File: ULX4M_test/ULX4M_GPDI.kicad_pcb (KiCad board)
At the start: 4 copper layers, 60 x 74 mm, 24 parts, among them J1 DF40C-100DP-0.4V(51), J10 DF40C-100DP-0.4V(51), J11 DF40C-100DP-0.4V(51), J12 DF40C-100DP-0.4V(51), J2 DF40C-100DP-0.4V(51), J3 DF40C-100DP-0.4V(51), J4 DF40C-100DP-0.4V(51), J5 DF40C-100DS-0.4V(51), J6 DF40C-100DS-0.4V(51), J7 DF40C-100DS-0.4V(51), J8 DF40C-100DS-0.4V(51), J9 DF40C-100DP-0.4V(51), P1 HDMI-D, P2 HDMI-D, P3 HDMI-D, P4 HDMI-D

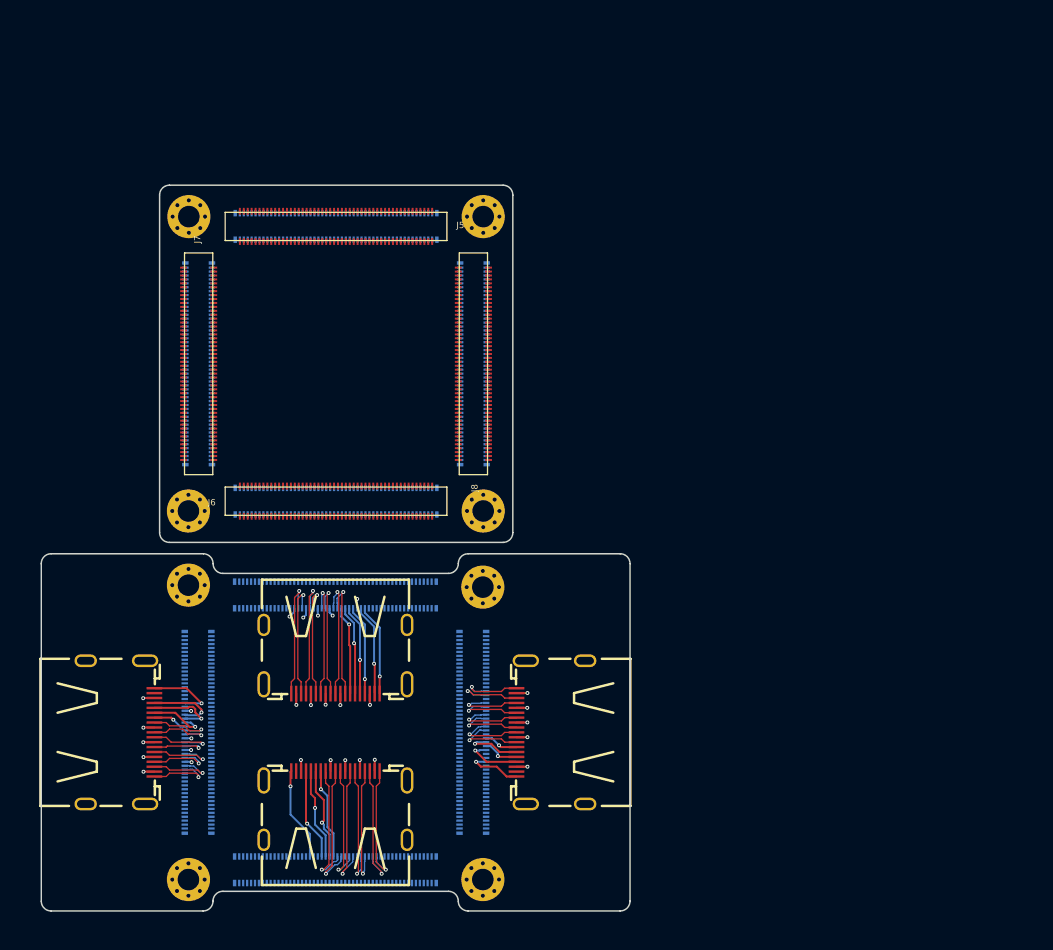
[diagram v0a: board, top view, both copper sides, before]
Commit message: Changing PCB size
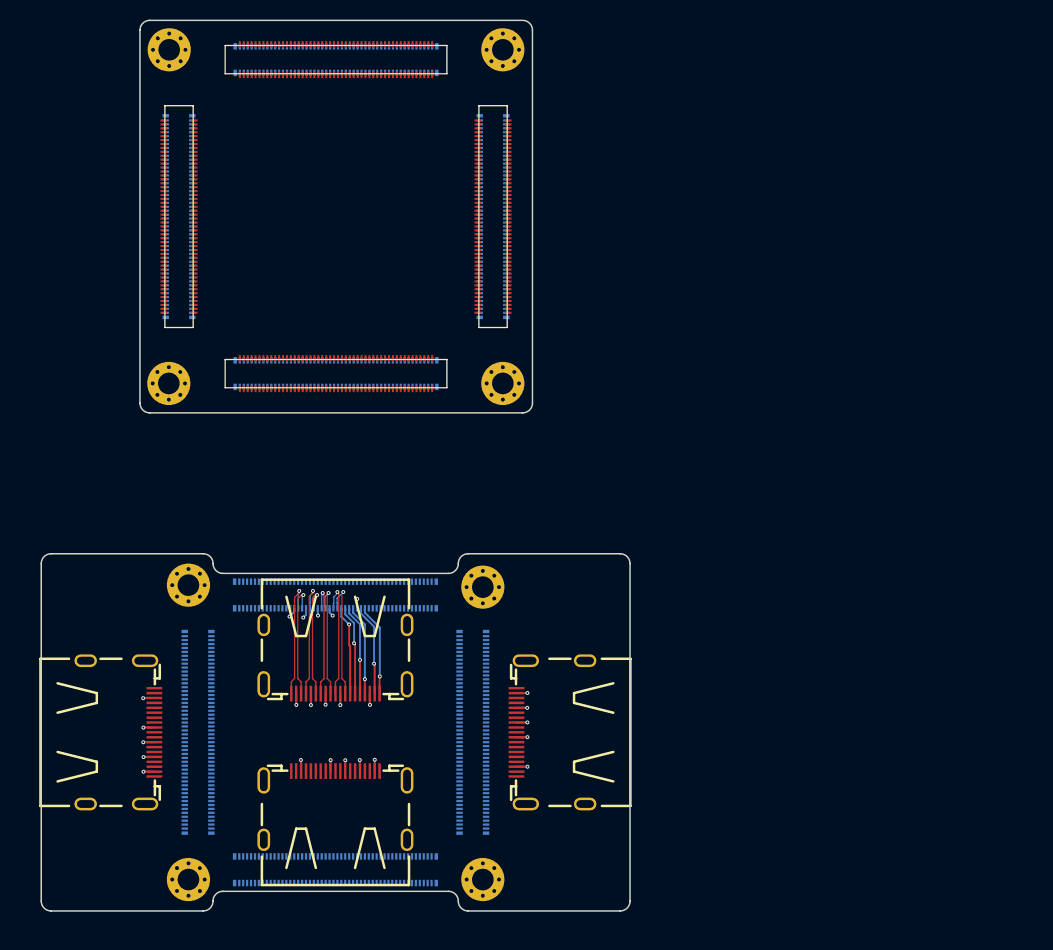
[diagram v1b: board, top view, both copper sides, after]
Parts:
- moved H5 17.1 mm to (83.1, 20.4)
- moved H7 17.1 mm to (117.1, 20.4)
- moved J5 17.0 mm to (100.1, 21.4)
- moved J9 17.0 mm to (100.1, 21.4)
- moved J11 15.1 mm to (84.1, 37.4)
- moved J12 15.1 mm to (116.1, 37.4)
- moved J7 15.1 mm to (84.1, 37.4)
- moved J8 15.1 mm to (116.1, 37.4)
- moved H6 13.2 mm to (83.0, 54.4)
- moved H8 13.2 mm to (117.1, 54.4)
- moved J10 13.0 mm to (100.1, 53.4)
- moved J6 13.0 mm to (100.1, 53.4)
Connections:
- J2 pad 36: (no net) -> P2_ETH-
- J2 pad 38: P2_ETH- -> +5V
- J2 pad 40: +5V -> GND
- J2 pad 42: GND -> P2_SDA
- J2 pad 44: P2_SDA -> P2_SCL
- J2 pad 46: P2_SCL -> P2_ETH+
- J2 pad 48: P2_ETH+ -> P2_CEC
- J2 pad 50: P2_CEC -> P2_CLK-
- J2 pad 52: P2_CLK- -> P2_CLK+
- J2 pad 54: P2_CLK+ -> GND
- J2 pad 56: (no net) -> P2_D0-
- J2 pad 58: P2_D0- -> P2_D0+
- J2 pad 60: P2_D0+ -> GND
- J2 pad 62: (no net) -> P2_D1-
- J2 pad 64: P2_D1- -> P2_D1+
- J2 pad 66: P2_D1+ -> GND
- J2 pad 68: (no net) -> P2_D2-
- J2 pad 70: P2_D2- -> P2_D2+
- J2 pad 72: P2_D2+ -> GND
- J3 pad 35: P3_ETH- -> (no net)
- J3 pad 36: (no net) -> P3_ETH-
- J3 pad 37: +5V -> (no net)
- J3 pad 38: (no net) -> +5V
- J3 pad 39: GND -> (no net)
- J3 pad 40: (no net) -> GND
- J3 pad 41: P3_SDA -> (no net)
- J3 pad 42: (no net) -> P3_SDA
- J3 pad 43: P3_SCL -> (no net)
- J3 pad 44: (no net) -> P3_SCL
- J3 pad 45: P3_ETH+ -> (no net)
- J3 pad 46: (no net) -> P3_ETH+
- J3 pad 47: P3_CEC -> (no net)
- J3 pad 48: (no net) -> P3_CEC
- J3 pad 49: P3_CLK- -> (no net)
- J3 pad 50: (no net) -> P3_CLK-
- J3 pad 51: P3_CLK+ -> (no net)
- J3 pad 52: (no net) -> P3_CLK+
- J3 pad 53: GND -> (no net)
- J3 pad 54: (no net) -> GND
- J3 pad 55: P3_D0- -> (no net)
- J3 pad 56: (no net) -> P3_D0-
- J3 pad 57: P3_D0+ -> (no net)
- J3 pad 58: (no net) -> P3_D0+
- J3 pad 59: GND -> (no net)
- J3 pad 60: (no net) -> GND
- J3 pad 61: P3_D1- -> (no net)
- J3 pad 62: (no net) -> P3_D1-
- J3 pad 63: P3_D1+ -> (no net)
- J3 pad 64: (no net) -> P3_D1+
- J3 pad 65: GND -> (no net)
- J3 pad 66: (no net) -> GND
- J3 pad 67: P3_D2- -> (no net)
- J3 pad 68: (no net) -> P3_D2-
- J3 pad 69: P3_D2+ -> (no net)
- J3 pad 70: (no net) -> P3_D2+
- J3 pad 71: GND -> (no net)
- J3 pad 72: (no net) -> GND
- J4 pad 35: P4_ETH- -> (no net)
- J4 pad 36: (no net) -> P4_ETH-
- J4 pad 37: +5V -> (no net)
- J4 pad 38: (no net) -> +5V
- J4 pad 39: GND -> (no net)
- J4 pad 40: (no net) -> GND
- J4 pad 41: P4_SDA -> (no net)
- J4 pad 42: (no net) -> P4_SDA
- J4 pad 43: P4_SCL -> (no net)
- J4 pad 44: (no net) -> P4_SCL
- J4 pad 45: P4_ETH+ -> (no net)
- J4 pad 46: (no net) -> P4_ETH+
- J4 pad 47: P4_CEC -> (no net)
- J4 pad 48: (no net) -> P4_CEC
- J4 pad 49: GND -> (no net)
- J4 pad 50: (no net) -> GND
- J4 pad 51: P4_CLK- -> (no net)
- J4 pad 52: (no net) -> P4_CLK-
- J4 pad 53: P4_CLK+ -> (no net)
- J4 pad 54: (no net) -> P4_CLK+
- J4 pad 55: GND -> (no net)
- J4 pad 56: (no net) -> GND
- J4 pad 57: P4_D0- -> (no net)
- J4 pad 58: (no net) -> P4_D0-
- J4 pad 59: P4_D0+ -> (no net)
- J4 pad 60: (no net) -> P4_D0+
- J4 pad 61: GND -> (no net)
- J4 pad 62: (no net) -> GND
- J4 pad 63: P4_D1- -> (no net)
- J4 pad 64: (no net) -> P4_D1-
- J4 pad 65: P4_D1+ -> (no net)
- J4 pad 66: (no net) -> P4_D1+
- J4 pad 67: GND -> (no net)
- J4 pad 68: (no net) -> GND
- J4 pad 69: P4_D2- -> (no net)
- J4 pad 70: (no net) -> P4_D2-
- J4 pad 71: P4_D2+ -> (no net)
- J4 pad 72: (no net) -> P4_D2+
- J4 pad 73: GND -> (no net)
- J4 pad 74: (no net) -> GND
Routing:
- net P2_CLK+: track 13.4 -> 0.00 mm, vias 1 -> 0
- net P2_D2-: track 13.1 -> 0.00 mm, vias 1 -> 0
- net P2_CLK-: track 13.0 -> 0.00 mm, vias 1 -> 0
- net P2_D0+: track 13.0 -> 0.00 mm, vias 1 -> 0
- net P2_D1-: track 12.6 -> 0.00 mm, vias 1 -> 0
- net P2_D2+: track 12.6 -> 0.00 mm, vias 1 -> 0
- net P2_D1+: track 12.5 -> 0.00 mm, vias 1 -> 0
- net P2_D0-: track 12.4 -> 0.00 mm, vias 1 -> 0
- net P2_ETH-: track 9.55 -> 0.00 mm, vias 1 -> 0
- net P2_ETH+: track 9.44 -> 0.00 mm, vias 1 -> 0
- net P2_SDA: track 9.36 -> 0.00 mm, vias 1 -> 0
- net P2_SCL: track 9.32 -> 0.00 mm, vias 1 -> 0
- net P2_CEC: track 9.23 -> 0.00 mm, vias 1 -> 0
- net P3_D1-: track 7.32 -> 0.00 mm, vias 1 -> 0
- net P4_D2-: track 7.31 -> 0.00 mm, vias 1 -> 0
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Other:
- board size 60 x 74 mm -> 60 x 90.8 mm

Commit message: Adding latest version
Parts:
- added mouse-bite-2mm-slot: VAL**, parts:mouse-bite-2mm-slot, F.Cu at (130.0, 89.9)
- added mouse-bite-2mm-slot: VAL**, parts:mouse-bite-2mm-slot, F.Cu at (130.0, 102.7)
- added mouse-bite-2mm-slot: VAL**, parts:mouse-bite-2mm-slot, F.Cu at (130.0, 73.7)
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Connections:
- J1 pad 1: (no net) -> GND
- J1 pad 10: (no net) -> GND
- J1 pad 100: (no net) -> GND
- J1 pad 11: (no net) -> GND
- J1 pad 12: (no net) -> GND
- J1 pad 13: (no net) -> GND
- J1 pad 14: (no net) -> GND
- J1 pad 15: (no net) -> GND
- J1 pad 16: (no net) -> GND
- J1 pad 17: (no net) -> GND
- J1 pad 18: (no net) -> GND
- J1 pad 19: (no net) -> GND
- J1 pad 2: (no net) -> GND
- J1 pad 20: (no net) -> GND
- J1 pad 21: (no net) -> GND
- J1 pad 22: (no net) -> GND
- J1 pad 23: (no net) -> GND
- J1 pad 24: (no net) -> GND
- J1 pad 25: (no net) -> GND
- J1 pad 26: (no net) -> GND
- J1 pad 27: (no net) -> GND
- J1 pad 28: (no net) -> GND
- J1 pad 29: (no net) -> GND
- J1 pad 3: (no net) -> GND
- J1 pad 30: (no net) -> GND
- J1 pad 31: (no net) -> GND
- J1 pad 32: (no net) -> GND
- J1 pad 33: (no net) -> GND
- J1 pad 34: (no net) -> GND
- J1 pad 35: (no net) -> GND
- J1 pad 37: (no net) -> GND
- J1 pad 39: (no net) -> GND
- J1 pad 4: (no net) -> GND
- J1 pad 41: (no net) -> GND
- J1 pad 43: (no net) -> GND
- J1 pad 45: (no net) -> GND
- J1 pad 47: (no net) -> GND
- J1 pad 49: (no net) -> GND
- J1 pad 5: (no net) -> GND
- J1 pad 51: (no net) -> GND
- J1 pad 53: (no net) -> GND
- J1 pad 55: (no net) -> GND
- J1 pad 57: (no net) -> GND
- J1 pad 59: (no net) -> GND
- J1 pad 6: (no net) -> GND
- J1 pad 61: (no net) -> GND
- J1 pad 63: (no net) -> GND
- J1 pad 65: (no net) -> GND
- J1 pad 67: (no net) -> GND
- J1 pad 69: (no net) -> GND
- J1 pad 7: (no net) -> GND
- J1 pad 71: (no net) -> GND
- J1 pad 73: (no net) -> GND
- J1 pad 74: (no net) -> GND
- J1 pad 75: (no net) -> GND
- J1 pad 76: (no net) -> GND
- J1 pad 77: (no net) -> GND
- J1 pad 78: (no net) -> GND
- J1 pad 79: (no net) -> GND
- J1 pad 8: (no net) -> GND
- J1 pad 80: (no net) -> GND
- J1 pad 81: (no net) -> GND
- J1 pad 82: (no net) -> GND
- J1 pad 83: (no net) -> GND
- J1 pad 84: (no net) -> GND
- J1 pad 85: (no net) -> GND
- J1 pad 86: (no net) -> GND
- J1 pad 87: (no net) -> GND
- J1 pad 88: (no net) -> GND
- J1 pad 89: (no net) -> GND
- J1 pad 9: (no net) -> GND
- J1 pad 90: (no net) -> GND
- J1 pad 91: (no net) -> GND
- J1 pad 92: (no net) -> GND
- J1 pad 93: (no net) -> GND
- J1 pad 94: (no net) -> GND
- J1 pad 95: (no net) -> GND
- J1 pad 96: (no net) -> GND
- J1 pad 97: (no net) -> GND
- J1 pad 98: (no net) -> GND
- J1 pad 99: (no net) -> GND
- J1 pad S1: (no net) -> GND
- J1 pad S2: (no net) -> GND
- J1 pad S3: (no net) -> GND
- J1 pad S4: (no net) -> GND
- J10 pad 1: (no net) -> GND
- J10 pad 10: (no net) -> GND
- J10 pad 100: (no net) -> GND
- J10 pad 11: (no net) -> GND
- J10 pad 12: (no net) -> GND
- J10 pad 13: (no net) -> GND
- J10 pad 14: (no net) -> GND
- J10 pad 15: (no net) -> GND
- J10 pad 16: (no net) -> GND
- J10 pad 17: (no net) -> GND
- J10 pad 18: (no net) -> GND
- J10 pad 19: (no net) -> GND
- J10 pad 2: (no net) -> GND
- J10 pad 20: (no net) -> GND
- J10 pad 21: (no net) -> GND
- J10 pad 22: (no net) -> GND
- J10 pad 23: (no net) -> GND
- J10 pad 24: (no net) -> GND
- J10 pad 25: (no net) -> GND
- J10 pad 26: (no net) -> GND
- J10 pad 27: (no net) -> GND
- J10 pad 28: (no net) -> GND
- J10 pad 29: (no net) -> GND
- J10 pad 3: (no net) -> GND
- J10 pad 30: (no net) -> GND
- J10 pad 31: (no net) -> GND
- J10 pad 32: (no net) -> GND
- J10 pad 33: (no net) -> GND
- J10 pad 34: (no net) -> GND
- J10 pad 35: (no net) -> GND
- J10 pad 36: (no net) -> GND
- J10 pad 37: (no net) -> GND
- J10 pad 38: (no net) -> GND
- J10 pad 39: (no net) -> GND
- J10 pad 4: (no net) -> GND
- J10 pad 40: (no net) -> GND
- J10 pad 41: (no net) -> GND
- J10 pad 42: (no net) -> GND
- J10 pad 43: (no net) -> GND
- J10 pad 44: (no net) -> GND
- J10 pad 45: (no net) -> GND
- J10 pad 46: (no net) -> GND
- J10 pad 47: (no net) -> GND
- J10 pad 48: (no net) -> GND
- J10 pad 49: (no net) -> GND
- J10 pad 5: (no net) -> GND
- J10 pad 50: (no net) -> GND
- J10 pad 51: (no net) -> GND
- J10 pad 52: (no net) -> GND
- J10 pad 53: (no net) -> GND
- J10 pad 54: (no net) -> GND
- J10 pad 55: (no net) -> GND
- J10 pad 56: (no net) -> GND
- J10 pad 57: (no net) -> GND
- J10 pad 58: (no net) -> GND
- J10 pad 59: (no net) -> GND
- J10 pad 6: (no net) -> GND
- J10 pad 60: (no net) -> GND
- J10 pad 61: (no net) -> GND
- J10 pad 62: (no net) -> GND
- J10 pad 63: (no net) -> GND
- J10 pad 64: (no net) -> GND
- J10 pad 65: (no net) -> GND
- J10 pad 66: (no net) -> GND
- J10 pad 67: (no net) -> GND
- J10 pad 68: (no net) -> GND
- J10 pad 69: (no net) -> GND
- J10 pad 7: (no net) -> GND
- J10 pad 70: (no net) -> GND
- J10 pad 71: (no net) -> GND
- J10 pad 72: (no net) -> GND
- J10 pad 73: (no net) -> GND
- J10 pad 74: (no net) -> GND
- J10 pad 75: (no net) -> GND
- J10 pad 76: (no net) -> GND
- J10 pad 77: (no net) -> GND
- J10 pad 78: (no net) -> GND
- J10 pad 79: (no net) -> GND
- J10 pad 8: (no net) -> GND
- J10 pad 80: (no net) -> GND
- J10 pad 81: (no net) -> GND
- J10 pad 82: (no net) -> GND
- J10 pad 83: (no net) -> GND
- J10 pad 84: (no net) -> GND
- J10 pad 85: (no net) -> GND
- J10 pad 86: (no net) -> GND
- J10 pad 87: (no net) -> GND
- J10 pad 88: (no net) -> GND
- J10 pad 89: (no net) -> GND
- J10 pad 9: (no net) -> GND
- J10 pad 90: (no net) -> GND
- J10 pad 91: (no net) -> GND
- J10 pad 92: (no net) -> GND
- J10 pad 93: (no net) -> GND
- J10 pad 94: (no net) -> GND
- J10 pad 95: (no net) -> GND
- J10 pad 96: (no net) -> GND
- J10 pad 97: (no net) -> GND
- J10 pad 98: (no net) -> GND
- J10 pad 99: (no net) -> GND
- J10 pad S1: (no net) -> GND
- J10 pad S2: (no net) -> GND
- J10 pad S3: (no net) -> GND
- J10 pad S4: (no net) -> GND
- J11 pad 1: (no net) -> GND
- J11 pad 10: (no net) -> GND
- J11 pad 100: (no net) -> GND
- J11 pad 11: (no net) -> GND
- J11 pad 12: (no net) -> GND
- J11 pad 13: (no net) -> GND
- J11 pad 14: (no net) -> GND
- J11 pad 15: (no net) -> GND
- J11 pad 16: (no net) -> GND
- J11 pad 17: (no net) -> GND
- J11 pad 18: (no net) -> GND
- J11 pad 19: (no net) -> GND
- J11 pad 2: (no net) -> GND
- J11 pad 20: (no net) -> GND
- J11 pad 21: (no net) -> GND
- J11 pad 22: (no net) -> GND
- J11 pad 23: (no net) -> GND
- J11 pad 24: (no net) -> GND
- J11 pad 25: (no net) -> GND
- J11 pad 26: (no net) -> GND
- J11 pad 27: (no net) -> GND
- J11 pad 28: (no net) -> GND
- J11 pad 29: (no net) -> GND
- J11 pad 3: (no net) -> GND
- J11 pad 30: (no net) -> GND
- J11 pad 31: (no net) -> GND
- J11 pad 32: (no net) -> GND
- J11 pad 33: (no net) -> GND
- J11 pad 34: (no net) -> GND
- J11 pad 35: (no net) -> GND
- J11 pad 36: (no net) -> GND
- J11 pad 37: (no net) -> GND
- J11 pad 38: (no net) -> GND
- J11 pad 39: (no net) -> GND
- J11 pad 4: (no net) -> GND
- J11 pad 40: (no net) -> GND
- J11 pad 41: (no net) -> GND
- J11 pad 42: (no net) -> GND
- J11 pad 43: (no net) -> GND
- J11 pad 44: (no net) -> GND
- J11 pad 45: (no net) -> GND
- J11 pad 46: (no net) -> GND
- J11 pad 47: (no net) -> GND
- J11 pad 48: (no net) -> GND
- J11 pad 49: (no net) -> GND
- J11 pad 5: (no net) -> GND
- J11 pad 50: (no net) -> GND
- J11 pad 51: (no net) -> GND
- J11 pad 52: (no net) -> GND
- J11 pad 53: (no net) -> GND
- J11 pad 54: (no net) -> GND
- J11 pad 55: (no net) -> GND
- J11 pad 56: (no net) -> GND
- J11 pad 57: (no net) -> GND
- J11 pad 58: (no net) -> GND
- J11 pad 59: (no net) -> GND
- J11 pad 6: (no net) -> GND
- J11 pad 60: (no net) -> GND
- J11 pad 61: (no net) -> GND
- J11 pad 62: (no net) -> GND
- J11 pad 63: (no net) -> GND
- J11 pad 64: (no net) -> GND
- J11 pad 65: (no net) -> GND
- J11 pad 66: (no net) -> GND
- J11 pad 67: (no net) -> GND
- J11 pad 68: (no net) -> GND
- J11 pad 69: (no net) -> GND
- J11 pad 7: (no net) -> GND
- J11 pad 70: (no net) -> GND
- J11 pad 71: (no net) -> GND
- J11 pad 72: (no net) -> GND
- J11 pad 73: (no net) -> GND
- J11 pad 74: (no net) -> GND
- J11 pad 75: (no net) -> GND
- J11 pad 76: (no net) -> GND
- J11 pad 77: (no net) -> GND
- J11 pad 78: (no net) -> GND
- J11 pad 79: (no net) -> GND
- J11 pad 8: (no net) -> GND
- J11 pad 80: (no net) -> GND
- J11 pad 81: (no net) -> GND
- J11 pad 82: (no net) -> GND
- J11 pad 83: (no net) -> GND
- J11 pad 84: (no net) -> GND
- J11 pad 85: (no net) -> GND
- J11 pad 86: (no net) -> GND
- J11 pad 87: (no net) -> GND
- J11 pad 88: (no net) -> GND
- J11 pad 89: (no net) -> GND
- J11 pad 9: (no net) -> GND
- J11 pad 90: (no net) -> GND
- J11 pad 91: (no net) -> GND
- J11 pad 92: (no net) -> GND
- J11 pad 93: (no net) -> GND
- J11 pad 94: (no net) -> GND
- J11 pad 95: (no net) -> GND
- J11 pad 96: (no net) -> GND
- J11 pad 97: (no net) -> GND
- J11 pad 98: (no net) -> GND
- J11 pad 99: (no net) -> GND
- J11 pad S1: (no net) -> GND
- J11 pad S2: (no net) -> GND
- J11 pad S3: (no net) -> GND
- J11 pad S4: (no net) -> GND
- J12 pad 1: (no net) -> GND
- J12 pad 10: (no net) -> GND
- J12 pad 100: (no net) -> GND
- J12 pad 11: (no net) -> GND
- J12 pad 12: (no net) -> GND
- J12 pad 13: (no net) -> GND
- J12 pad 14: (no net) -> GND
- J12 pad 15: (no net) -> GND
- J12 pad 16: (no net) -> GND
- J12 pad 17: (no net) -> GND
- J12 pad 18: (no net) -> GND
- J12 pad 19: (no net) -> GND
- J12 pad 2: (no net) -> GND
- J12 pad 20: (no net) -> GND
- J12 pad 21: (no net) -> GND
- J12 pad 22: (no net) -> GND
- J12 pad 23: (no net) -> GND
- J12 pad 24: (no net) -> GND
- J12 pad 25: (no net) -> GND
- J12 pad 26: (no net) -> GND
- J12 pad 27: (no net) -> GND
- J12 pad 28: (no net) -> GND
- J12 pad 29: (no net) -> GND
- J12 pad 3: (no net) -> GND
- J12 pad 30: (no net) -> GND
- J12 pad 31: (no net) -> GND
- J12 pad 32: (no net) -> GND
- J12 pad 33: (no net) -> GND
- J12 pad 34: (no net) -> GND
- J12 pad 35: (no net) -> GND
- J12 pad 36: (no net) -> GND
- J12 pad 37: (no net) -> GND
- J12 pad 38: (no net) -> GND
- J12 pad 39: (no net) -> GND
- J12 pad 4: (no net) -> GND
- J12 pad 40: (no net) -> GND
- J12 pad 41: (no net) -> GND
- J12 pad 42: (no net) -> GND
- J12 pad 43: (no net) -> GND
- J12 pad 44: (no net) -> GND
- J12 pad 45: (no net) -> GND
- J12 pad 46: (no net) -> GND
- J12 pad 47: (no net) -> GND
- J12 pad 48: (no net) -> GND
- J12 pad 49: (no net) -> GND
- J12 pad 5: (no net) -> GND
- J12 pad 50: (no net) -> GND
- J12 pad 51: (no net) -> GND
- J12 pad 52: (no net) -> GND
- J12 pad 53: (no net) -> GND
- J12 pad 54: (no net) -> GND
- J12 pad 55: (no net) -> GND
- J12 pad 56: (no net) -> GND
- J12 pad 57: (no net) -> GND
- J12 pad 58: (no net) -> GND
- J12 pad 59: (no net) -> GND
- J12 pad 6: (no net) -> GND
- J12 pad 60: (no net) -> GND
- J12 pad 61: (no net) -> GND
- J12 pad 62: (no net) -> GND
- J12 pad 63: (no net) -> GND
- J12 pad 64: (no net) -> GND
- J12 pad 65: (no net) -> GND
- J12 pad 66: (no net) -> GND
- J12 pad 67: (no net) -> GND
- J12 pad 68: (no net) -> GND
- J12 pad 69: (no net) -> GND
- J12 pad 7: (no net) -> GND
- J12 pad 70: (no net) -> GND
- J12 pad 71: (no net) -> GND
- J12 pad 72: (no net) -> GND
- J12 pad 73: (no net) -> GND
- J12 pad 74: (no net) -> GND
- J12 pad 75: (no net) -> GND
- J12 pad 76: (no net) -> GND
- J12 pad 77: (no net) -> GND
- J12 pad 78: (no net) -> GND
- J12 pad 79: (no net) -> GND
- J12 pad 8: (no net) -> GND
- J12 pad 80: (no net) -> GND
- J12 pad 81: (no net) -> GND
- J12 pad 82: (no net) -> GND
- J12 pad 83: (no net) -> GND
- J12 pad 84: (no net) -> GND
- J12 pad 85: (no net) -> GND
- J12 pad 86: (no net) -> GND
- J12 pad 87: (no net) -> GND
- J12 pad 88: (no net) -> GND
- J12 pad 89: (no net) -> GND
- J12 pad 9: (no net) -> GND
- J12 pad 90: (no net) -> GND
- J12 pad 91: (no net) -> GND
- J12 pad 92: (no net) -> GND
- J12 pad 93: (no net) -> GND
- J12 pad 94: (no net) -> GND
- J12 pad 95: (no net) -> GND
- J12 pad 96: (no net) -> GND
- J12 pad 97: (no net) -> GND
- J12 pad 98: (no net) -> GND
- J12 pad 99: (no net) -> GND
- J12 pad S1: (no net) -> GND
- J12 pad S2: (no net) -> GND
- J12 pad S3: (no net) -> GND
- J12 pad S4: (no net) -> GND
- J2 pad 1: (no net) -> GND
- J2 pad 10: (no net) -> GND
- J2 pad 100: (no net) -> GND
- J2 pad 11: (no net) -> GND
- J2 pad 12: (no net) -> GND
- J2 pad 13: (no net) -> GND
- J2 pad 14: (no net) -> GND
- J2 pad 15: (no net) -> GND
- J2 pad 16: (no net) -> GND
- J2 pad 17: (no net) -> GND
- J2 pad 18: (no net) -> GND
- J2 pad 19: (no net) -> GND
- J2 pad 2: (no net) -> GND
- J2 pad 20: (no net) -> GND
- J2 pad 21: (no net) -> GND
- J2 pad 22: (no net) -> GND
- J2 pad 23: (no net) -> GND
- J2 pad 24: (no net) -> GND
- J2 pad 25: (no net) -> GND
- J2 pad 26: (no net) -> GND
- J2 pad 27: (no net) -> GND
- J2 pad 28: (no net) -> GND
- J2 pad 29: (no net) -> GND
- J2 pad 3: (no net) -> GND
- J2 pad 30: (no net) -> GND
- J2 pad 31: (no net) -> GND
- J2 pad 32: (no net) -> GND
- J2 pad 33: (no net) -> GND
- J2 pad 34: (no net) -> GND
- J2 pad 35: (no net) -> GND
- J2 pad 37: (no net) -> GND
- J2 pad 39: (no net) -> GND
- J2 pad 4: (no net) -> GND
- J2 pad 41: (no net) -> GND
- J2 pad 43: (no net) -> GND
- J2 pad 45: (no net) -> GND
- J2 pad 47: (no net) -> GND
- J2 pad 49: (no net) -> GND
- J2 pad 5: (no net) -> GND
- J2 pad 51: (no net) -> GND
- J2 pad 53: (no net) -> GND
- J2 pad 55: (no net) -> GND
- J2 pad 57: (no net) -> GND
- J2 pad 59: (no net) -> GND
- J2 pad 6: (no net) -> GND
- J2 pad 61: (no net) -> GND
- J2 pad 63: (no net) -> GND
- J2 pad 65: (no net) -> GND
- J2 pad 67: (no net) -> GND
- J2 pad 69: (no net) -> GND
- J2 pad 7: (no net) -> GND
- J2 pad 71: (no net) -> GND
- J2 pad 73: (no net) -> GND
- J2 pad 74: (no net) -> GND
- J2 pad 75: (no net) -> GND
- J2 pad 76: (no net) -> GND
- J2 pad 77: (no net) -> GND
- J2 pad 78: (no net) -> GND
- J2 pad 79: (no net) -> GND
- J2 pad 8: (no net) -> GND
- J2 pad 80: (no net) -> GND
- J2 pad 81: (no net) -> GND
- J2 pad 82: (no net) -> GND
- J2 pad 83: (no net) -> GND
- J2 pad 84: (no net) -> GND
- J2 pad 85: (no net) -> GND
- J2 pad 86: (no net) -> GND
- J2 pad 87: (no net) -> GND
- J2 pad 88: (no net) -> GND
- J2 pad 89: (no net) -> GND
- J2 pad 9: (no net) -> GND
- J2 pad 90: (no net) -> GND
- J2 pad 91: (no net) -> GND
- J2 pad 92: (no net) -> GND
- J2 pad 93: (no net) -> GND
- J2 pad 94: (no net) -> GND
- J2 pad 95: (no net) -> GND
- J2 pad 96: (no net) -> GND
- J2 pad 97: (no net) -> GND
- J2 pad 98: (no net) -> GND
- J2 pad 99: (no net) -> GND
- J2 pad S1: (no net) -> GND
- J2 pad S2: (no net) -> GND
- J2 pad S3: (no net) -> GND
- J2 pad S4: (no net) -> GND
- J3 pad 1: (no net) -> GND
- J3 pad 10: (no net) -> GND
- J3 pad 100: (no net) -> GND
- J3 pad 11: (no net) -> GND
- J3 pad 12: (no net) -> GND
- J3 pad 13: (no net) -> GND
- J3 pad 14: (no net) -> GND
- J3 pad 15: (no net) -> GND
- J3 pad 16: (no net) -> GND
- J3 pad 17: (no net) -> GND
- J3 pad 18: (no net) -> GND
- J3 pad 19: (no net) -> GND
- J3 pad 2: (no net) -> GND
- J3 pad 20: (no net) -> GND
- J3 pad 21: (no net) -> GND
- J3 pad 22: (no net) -> GND
- J3 pad 23: (no net) -> GND
- J3 pad 24: (no net) -> GND
- J3 pad 25: (no net) -> GND
- J3 pad 26: (no net) -> GND
- J3 pad 27: (no net) -> GND
- J3 pad 28: (no net) -> GND
- J3 pad 29: (no net) -> GND
- J3 pad 3: (no net) -> GND
- J3 pad 30: (no net) -> GND
- J3 pad 31: (no net) -> GND
- J3 pad 32: (no net) -> GND
- J3 pad 33: (no net) -> GND
- J3 pad 34: (no net) -> GND
- J3 pad 35: (no net) -> GND
- J3 pad 37: (no net) -> GND
- J3 pad 39: (no net) -> GND
- J3 pad 4: (no net) -> GND
- J3 pad 41: (no net) -> GND
- J3 pad 43: (no net) -> GND
- J3 pad 45: (no net) -> GND
- J3 pad 47: (no net) -> GND
- J3 pad 49: (no net) -> GND
- J3 pad 5: (no net) -> GND
- J3 pad 51: (no net) -> GND
- J3 pad 53: (no net) -> GND
- J3 pad 55: (no net) -> GND
- J3 pad 57: (no net) -> GND
- J3 pad 59: (no net) -> GND
- J3 pad 6: (no net) -> GND
- J3 pad 61: (no net) -> GND
- J3 pad 63: (no net) -> GND
- J3 pad 65: (no net) -> GND
- J3 pad 67: (no net) -> GND
- J3 pad 69: (no net) -> GND
- J3 pad 7: (no net) -> GND
- J3 pad 71: (no net) -> GND
- J3 pad 73: (no net) -> GND
- J3 pad 74: (no net) -> GND
- J3 pad 75: (no net) -> GND
- J3 pad 76: (no net) -> GND
- J3 pad 77: (no net) -> GND
- J3 pad 78: (no net) -> GND
- J3 pad 79: (no net) -> GND
- J3 pad 8: (no net) -> GND
- J3 pad 80: (no net) -> GND
- J3 pad 81: (no net) -> GND
- J3 pad 82: (no net) -> GND
- J3 pad 83: (no net) -> GND
- J3 pad 84: (no net) -> GND
- J3 pad 85: (no net) -> GND
- J3 pad 86: (no net) -> GND
- J3 pad 87: (no net) -> GND
- J3 pad 88: (no net) -> GND
- J3 pad 89: (no net) -> GND
- J3 pad 9: (no net) -> GND
- J3 pad 90: (no net) -> GND
- J3 pad 91: (no net) -> GND
- J3 pad 92: (no net) -> GND
- J3 pad 93: (no net) -> GND
- J3 pad 94: (no net) -> GND
- J3 pad 95: (no net) -> GND
- J3 pad 96: (no net) -> GND
- J3 pad 97: (no net) -> GND
- J3 pad 98: (no net) -> GND
- J3 pad 99: (no net) -> GND
- J3 pad S1: (no net) -> GND
- J3 pad S2: (no net) -> GND
- J3 pad S3: (no net) -> GND
- J3 pad S4: (no net) -> GND
- J4 pad 1: (no net) -> GND
- J4 pad 10: (no net) -> GND
- J4 pad 100: (no net) -> GND
- J4 pad 11: (no net) -> GND
- J4 pad 12: (no net) -> GND
- J4 pad 13: (no net) -> GND
- J4 pad 14: (no net) -> GND
- J4 pad 15: (no net) -> GND
- J4 pad 16: (no net) -> GND
- J4 pad 17: (no net) -> GND
- J4 pad 18: (no net) -> GND
- J4 pad 19: (no net) -> GND
- J4 pad 2: (no net) -> GND
- J4 pad 20: (no net) -> GND
- J4 pad 21: (no net) -> GND
- J4 pad 22: (no net) -> GND
- J4 pad 23: (no net) -> GND
- J4 pad 24: (no net) -> GND
- J4 pad 25: (no net) -> GND
- J4 pad 26: (no net) -> GND
- J4 pad 27: (no net) -> GND
- J4 pad 28: (no net) -> GND
- J4 pad 29: (no net) -> GND
- J4 pad 3: (no net) -> GND
- J4 pad 30: (no net) -> GND
- J4 pad 31: (no net) -> GND
- J4 pad 32: (no net) -> GND
- J4 pad 33: (no net) -> GND
- J4 pad 34: (no net) -> GND
- J4 pad 35: (no net) -> GND
- J4 pad 37: (no net) -> GND
- J4 pad 39: (no net) -> GND
- J4 pad 4: (no net) -> GND
- J4 pad 41: (no net) -> GND
- J4 pad 43: (no net) -> GND
- J4 pad 45: (no net) -> GND
- J4 pad 47: (no net) -> GND
- J4 pad 49: (no net) -> GND
- J4 pad 5: (no net) -> GND
- J4 pad 51: (no net) -> GND
- J4 pad 53: (no net) -> GND
- J4 pad 55: (no net) -> GND
- J4 pad 57: (no net) -> GND
- J4 pad 59: (no net) -> GND
- J4 pad 6: (no net) -> GND
- J4 pad 61: (no net) -> GND
- J4 pad 63: (no net) -> GND
- J4 pad 65: (no net) -> GND
- J4 pad 67: (no net) -> GND
- J4 pad 69: (no net) -> GND
- J4 pad 7: (no net) -> GND
- J4 pad 71: (no net) -> GND
- J4 pad 73: (no net) -> GND
- J4 pad 75: (no net) -> GND
- J4 pad 76: (no net) -> GND
- J4 pad 77: (no net) -> GND
- J4 pad 78: (no net) -> GND
- J4 pad 79: (no net) -> GND
- J4 pad 8: (no net) -> GND
- J4 pad 80: (no net) -> GND
- J4 pad 81: (no net) -> GND
- J4 pad 82: (no net) -> GND
- J4 pad 83: (no net) -> GND
- J4 pad 84: (no net) -> GND
- J4 pad 85: (no net) -> GND
- J4 pad 86: (no net) -> GND
- J4 pad 87: (no net) -> GND
- J4 pad 88: (no net) -> GND
- J4 pad 89: (no net) -> GND
- J4 pad 9: (no net) -> GND
- J4 pad 90: (no net) -> GND
- J4 pad 91: (no net) -> GND
- J4 pad 92: (no net) -> GND
- J4 pad 93: (no net) -> GND
- J4 pad 94: (no net) -> GND
- J4 pad 95: (no net) -> GND
- J4 pad 96: (no net) -> GND
- J4 pad 97: (no net) -> GND
- J4 pad 98: (no net) -> GND
- J4 pad 99: (no net) -> GND
- J4 pad S1: (no net) -> GND
- J4 pad S2: (no net) -> GND
- J4 pad S3: (no net) -> GND
- J4 pad S4: (no net) -> GND
- J5 pad 1: (no net) -> GND
- J5 pad 10: (no net) -> GND
- J5 pad 100: (no net) -> GND
- J5 pad 11: (no net) -> GND
- J5 pad 12: (no net) -> GND
- J5 pad 13: (no net) -> GND
- J5 pad 14: (no net) -> GND
- J5 pad 15: (no net) -> GND
- J5 pad 16: (no net) -> GND
- J5 pad 17: (no net) -> GND
- J5 pad 18: (no net) -> GND
- J5 pad 19: (no net) -> GND
- J5 pad 2: (no net) -> GND
- J5 pad 20: (no net) -> GND
- J5 pad 21: (no net) -> GND
- J5 pad 22: (no net) -> GND
- J5 pad 23: (no net) -> GND
- J5 pad 24: (no net) -> GND
- J5 pad 25: (no net) -> GND
- J5 pad 26: (no net) -> GND
- J5 pad 27: (no net) -> GND
- J5 pad 28: (no net) -> GND
- J5 pad 29: (no net) -> GND
- J5 pad 3: (no net) -> GND
- J5 pad 30: (no net) -> GND
- J5 pad 31: (no net) -> GND
- J5 pad 32: (no net) -> GND
- J5 pad 33: (no net) -> GND
- J5 pad 34: (no net) -> GND
- J5 pad 35: (no net) -> GND
- J5 pad 36: (no net) -> GND
- J5 pad 37: (no net) -> GND
- J5 pad 38: (no net) -> GND
- J5 pad 39: (no net) -> GND
- J5 pad 4: (no net) -> GND
- J5 pad 40: (no net) -> GND
- J5 pad 41: (no net) -> GND
- J5 pad 42: (no net) -> GND
- J5 pad 43: (no net) -> GND
- J5 pad 44: (no net) -> GND
- J5 pad 45: (no net) -> GND
- J5 pad 46: (no net) -> GND
- J5 pad 47: (no net) -> GND
- J5 pad 48: (no net) -> GND
- J5 pad 49: (no net) -> GND
- J5 pad 5: (no net) -> GND
- J5 pad 50: (no net) -> /C1_C-
- J5 pad 51: (no net) -> GND
- J5 pad 52: (no net) -> /C1_C+
- J5 pad 53: (no net) -> GND
- J5 pad 54: (no net) -> GND
- J5 pad 55: (no net) -> GND
- J5 pad 56: (no net) -> /C1_D0-
- J5 pad 57: (no net) -> GND
- J5 pad 58: (no net) -> /C1_D0+
- J5 pad 59: (no net) -> GND
- J5 pad 6: (no net) -> GND
- J5 pad 60: (no net) -> GND
- J5 pad 61: (no net) -> GND
- J5 pad 62: (no net) -> /C1_D1-
- J5 pad 63: (no net) -> GND
- J5 pad 64: (no net) -> /C1_D1+
- J5 pad 65: (no net) -> GND
- J5 pad 66: (no net) -> GND
- J5 pad 67: (no net) -> GND
- J5 pad 68: (no net) -> /C1_D2-
- J5 pad 69: (no net) -> GND
- J5 pad 7: (no net) -> GND
- J5 pad 70: (no net) -> /C1_D2+
- J5 pad 71: (no net) -> GND
- J5 pad 72: (no net) -> GND
- J5 pad 73: (no net) -> GND
- J5 pad 74: (no net) -> GND
- J5 pad 75: (no net) -> GND
- J5 pad 76: (no net) -> GND
- J5 pad 77: (no net) -> GND
- J5 pad 78: (no net) -> GND
- J5 pad 79: (no net) -> GND
- J5 pad 8: (no net) -> GND
- J5 pad 80: (no net) -> GND
- J5 pad 81: (no net) -> GND
- J5 pad 82: (no net) -> GND
- J5 pad 83: (no net) -> GND
- J5 pad 84: (no net) -> GND
- J5 pad 85: (no net) -> GND
- J5 pad 86: (no net) -> GND
- J5 pad 87: (no net) -> GND
- J5 pad 88: (no net) -> GND
- J5 pad 89: (no net) -> GND
- J5 pad 9: (no net) -> GND
- J5 pad 90: (no net) -> GND
- J5 pad 91: (no net) -> GND
- J5 pad 92: (no net) -> GND
- J5 pad 93: (no net) -> GND
- J5 pad 94: (no net) -> GND
- J5 pad 95: (no net) -> GND
- J5 pad 96: (no net) -> GND
- J5 pad 97: (no net) -> GND
- J5 pad 98: (no net) -> GND
- J5 pad 99: (no net) -> GND
- J6 pad 1: (no net) -> GND
- J6 pad 10: (no net) -> GND
- J6 pad 100: (no net) -> GND
- J6 pad 11: (no net) -> GND
- J6 pad 12: (no net) -> GND
- J6 pad 13: (no net) -> GND
- J6 pad 14: (no net) -> GND
- J6 pad 15: (no net) -> GND
- J6 pad 16: (no net) -> GND
- J6 pad 17: (no net) -> GND
- J6 pad 18: (no net) -> GND
- J6 pad 19: (no net) -> GND
- J6 pad 2: (no net) -> GND
- J6 pad 20: (no net) -> GND
- J6 pad 21: (no net) -> GND
- J6 pad 22: (no net) -> GND
- J6 pad 23: (no net) -> GND
- J6 pad 24: (no net) -> GND
- J6 pad 25: (no net) -> GND
- J6 pad 26: (no net) -> GND
- J6 pad 27: (no net) -> GND
- J6 pad 28: (no net) -> GND
- J6 pad 29: (no net) -> GND
- J6 pad 3: (no net) -> GND
- J6 pad 30: (no net) -> GND
- J6 pad 31: (no net) -> GND
- J6 pad 32: (no net) -> GND
- J6 pad 33: (no net) -> GND
- J6 pad 34: (no net) -> GND
- J6 pad 35: (no net) -> GND
- J6 pad 36: (no net) -> GND
- J6 pad 37: (no net) -> GND
- J6 pad 38: (no net) -> GND
- J6 pad 39: (no net) -> GND
- J6 pad 4: (no net) -> GND
- J6 pad 40: (no net) -> GND
- J6 pad 41: (no net) -> GND
- J6 pad 42: (no net) -> GND
- J6 pad 43: (no net) -> GND
- J6 pad 44: (no net) -> GND
- J6 pad 45: (no net) -> GND
- J6 pad 46: (no net) -> GND
- J6 pad 47: (no net) -> GND
- J6 pad 48: (no net) -> GND
- J6 pad 49: (no net) -> GND
- J6 pad 5: (no net) -> GND
- J6 pad 50: (no net) -> /C1_C-
- J6 pad 51: (no net) -> GND
- J6 pad 52: (no net) -> /C1_C+
- J6 pad 53: (no net) -> GND
- J6 pad 54: (no net) -> GND
- J6 pad 55: (no net) -> GND
- J6 pad 56: (no net) -> /C1_D0-
- J6 pad 57: (no net) -> GND
- J6 pad 58: (no net) -> /C1_D0+
- J6 pad 59: (no net) -> GND
- J6 pad 6: (no net) -> GND
- J6 pad 60: (no net) -> GND
- J6 pad 61: (no net) -> GND
- J6 pad 62: (no net) -> /C1_D1-
- J6 pad 63: (no net) -> GND
- J6 pad 64: (no net) -> /C1_D1+
- J6 pad 65: (no net) -> GND
- J6 pad 66: (no net) -> GND
- J6 pad 67: (no net) -> GND
- J6 pad 68: (no net) -> /C1_D2-
- J6 pad 69: (no net) -> GND
- J6 pad 7: (no net) -> GND
- J6 pad 70: (no net) -> /C1_D2+
- J6 pad 71: (no net) -> GND
- J6 pad 72: (no net) -> GND
- J6 pad 73: (no net) -> GND
- J6 pad 74: (no net) -> GND
- J6 pad 75: (no net) -> GND
- J6 pad 76: (no net) -> GND
- J6 pad 77: (no net) -> GND
- J6 pad 78: (no net) -> GND
- J6 pad 79: (no net) -> GND
- J6 pad 8: (no net) -> GND
- J6 pad 80: (no net) -> GND
- J6 pad 81: (no net) -> GND
- J6 pad 82: (no net) -> GND
- J6 pad 83: (no net) -> GND
- J6 pad 84: (no net) -> GND
- J6 pad 85: (no net) -> GND
- J6 pad 86: (no net) -> GND
- J6 pad 87: (no net) -> GND
- J6 pad 88: (no net) -> GND
- J6 pad 89: (no net) -> GND
- J6 pad 9: (no net) -> GND
- J6 pad 90: (no net) -> GND
- J6 pad 91: (no net) -> GND
- J6 pad 92: (no net) -> GND
- J6 pad 93: (no net) -> GND
- J6 pad 94: (no net) -> GND
- J6 pad 95: (no net) -> GND
- J6 pad 96: (no net) -> GND
- J6 pad 97: (no net) -> GND
- J6 pad 98: (no net) -> GND
- J6 pad 99: (no net) -> GND
- J7 pad 1: (no net) -> GND
- J7 pad 10: (no net) -> GND
- J7 pad 100: (no net) -> GND
- J7 pad 11: (no net) -> GND
- J7 pad 12: (no net) -> GND
- J7 pad 13: (no net) -> GND
- J7 pad 14: (no net) -> GND
- J7 pad 15: (no net) -> GND
- J7 pad 16: (no net) -> GND
- J7 pad 17: (no net) -> GND
- J7 pad 18: (no net) -> GND
- J7 pad 19: (no net) -> GND
- J7 pad 2: (no net) -> GND
- J7 pad 20: (no net) -> GND
- J7 pad 21: (no net) -> GND
- J7 pad 22: (no net) -> GND
- J7 pad 23: (no net) -> GND
- J7 pad 24: (no net) -> GND
- J7 pad 25: (no net) -> GND
- J7 pad 26: (no net) -> GND
- J7 pad 27: (no net) -> GND
- J7 pad 28: (no net) -> GND
- J7 pad 29: (no net) -> GND
- J7 pad 3: (no net) -> GND
- J7 pad 30: (no net) -> GND
- J7 pad 31: (no net) -> GND
- J7 pad 32: (no net) -> GND
- J7 pad 33: (no net) -> GND
- J7 pad 34: (no net) -> GND
- J7 pad 35: (no net) -> GND
- J7 pad 36: (no net) -> GND
- J7 pad 37: (no net) -> GND
- J7 pad 38: (no net) -> GND
- J7 pad 39: (no net) -> GND
- J7 pad 4: (no net) -> GND
- J7 pad 40: (no net) -> GND
- J7 pad 41: (no net) -> GND
- J7 pad 42: (no net) -> GND
- J7 pad 43: (no net) -> GND
- J7 pad 44: (no net) -> GND
- J7 pad 45: (no net) -> GND
- J7 pad 46: (no net) -> GND
- J7 pad 47: (no net) -> GND
- J7 pad 48: (no net) -> GND
- J7 pad 49: (no net) -> GND
- J7 pad 5: (no net) -> GND
- J7 pad 50: (no net) -> /C2_C-
- J7 pad 51: (no net) -> GND
- J7 pad 52: (no net) -> /C2_C+
- J7 pad 53: (no net) -> GND
- J7 pad 54: (no net) -> GND
- J7 pad 55: (no net) -> GND
- J7 pad 56: (no net) -> /C2_D0-
- J7 pad 57: (no net) -> GND
- J7 pad 58: (no net) -> /C2_D0+
- J7 pad 59: (no net) -> GND
- J7 pad 6: (no net) -> GND
- J7 pad 60: (no net) -> GND
- J7 pad 61: (no net) -> GND
- J7 pad 62: (no net) -> /C2_D1-
- J7 pad 63: (no net) -> GND
- J7 pad 64: (no net) -> /C2_D1+
- J7 pad 65: (no net) -> GND
- J7 pad 66: (no net) -> GND
- J7 pad 67: (no net) -> GND
- J7 pad 68: (no net) -> /C2_D2-
- J7 pad 69: (no net) -> GND
- J7 pad 7: (no net) -> GND
- J7 pad 70: (no net) -> /C2_D2+
- J7 pad 71: (no net) -> GND
- J7 pad 72: (no net) -> GND
- J7 pad 73: (no net) -> GND
- J7 pad 74: (no net) -> GND
- J7 pad 75: (no net) -> GND
- J7 pad 76: (no net) -> GND
- J7 pad 77: (no net) -> GND
- J7 pad 78: (no net) -> GND
- J7 pad 79: (no net) -> GND
- J7 pad 8: (no net) -> GND
- J7 pad 80: (no net) -> GND
- J7 pad 81: (no net) -> GND
- J7 pad 82: (no net) -> GND
- J7 pad 83: (no net) -> GND
- J7 pad 84: (no net) -> GND
- J7 pad 85: (no net) -> GND
- J7 pad 86: (no net) -> GND
- J7 pad 87: (no net) -> GND
- J7 pad 88: (no net) -> GND
- J7 pad 89: (no net) -> GND
- J7 pad 9: (no net) -> GND
- J7 pad 90: (no net) -> GND
- J7 pad 91: (no net) -> GND
- J7 pad 92: (no net) -> GND
- J7 pad 93: (no net) -> GND
- J7 pad 94: (no net) -> GND
- J7 pad 95: (no net) -> GND
- J7 pad 96: (no net) -> GND
- J7 pad 97: (no net) -> GND
- J7 pad 98: (no net) -> GND
- J7 pad 99: (no net) -> GND
- J8 pad 1: (no net) -> GND
- J8 pad 10: (no net) -> GND
- J8 pad 100: (no net) -> GND
- J8 pad 11: (no net) -> GND
- J8 pad 12: (no net) -> GND
- J8 pad 13: (no net) -> GND
- J8 pad 14: (no net) -> GND
- J8 pad 15: (no net) -> GND
- J8 pad 16: (no net) -> GND
- J8 pad 17: (no net) -> GND
- J8 pad 18: (no net) -> GND
- J8 pad 19: (no net) -> GND
- J8 pad 2: (no net) -> GND
- J8 pad 20: (no net) -> GND
- J8 pad 21: (no net) -> GND
- J8 pad 22: (no net) -> GND
- J8 pad 23: (no net) -> GND
- J8 pad 24: (no net) -> GND
- J8 pad 25: (no net) -> GND
- J8 pad 26: (no net) -> GND
- J8 pad 27: (no net) -> GND
- J8 pad 28: (no net) -> GND
- J8 pad 29: (no net) -> GND
- J8 pad 3: (no net) -> GND
- J8 pad 30: (no net) -> GND
- J8 pad 31: (no net) -> GND
- J8 pad 32: (no net) -> GND
- J8 pad 33: (no net) -> GND
- J8 pad 34: (no net) -> GND
- J8 pad 35: (no net) -> GND
- J8 pad 36: (no net) -> GND
- J8 pad 37: (no net) -> GND
- J8 pad 38: (no net) -> GND
- J8 pad 39: (no net) -> GND
- J8 pad 4: (no net) -> GND
- J8 pad 40: (no net) -> GND
- J8 pad 41: (no net) -> GND
- J8 pad 42: (no net) -> GND
- J8 pad 43: (no net) -> GND
- J8 pad 44: (no net) -> GND
- J8 pad 45: (no net) -> GND
- J8 pad 46: (no net) -> GND
- J8 pad 47: (no net) -> GND
- J8 pad 48: (no net) -> GND
- J8 pad 49: (no net) -> GND
- J8 pad 5: (no net) -> GND
- J8 pad 50: (no net) -> /C2_C-
- J8 pad 51: (no net) -> GND
- J8 pad 52: (no net) -> /C2_C+
- J8 pad 53: (no net) -> GND
- J8 pad 54: (no net) -> GND
- J8 pad 55: (no net) -> GND
- J8 pad 56: (no net) -> /C2_D0-
- J8 pad 57: (no net) -> GND
- J8 pad 58: (no net) -> /C2_D0+
- J8 pad 59: (no net) -> GND
- J8 pad 6: (no net) -> GND
- J8 pad 60: (no net) -> GND
- J8 pad 61: (no net) -> GND
- J8 pad 62: (no net) -> /C2_D1-
- J8 pad 63: (no net) -> GND
- J8 pad 64: (no net) -> /C2_D1+
- J8 pad 65: (no net) -> GND
- J8 pad 66: (no net) -> GND
- J8 pad 67: (no net) -> GND
- J8 pad 68: (no net) -> /C2_D2-
- J8 pad 69: (no net) -> GND
- J8 pad 7: (no net) -> GND
- J8 pad 70: (no net) -> /C2_D2+
- J8 pad 71: (no net) -> GND
- J8 pad 72: (no net) -> GND
- J8 pad 73: (no net) -> GND
- J8 pad 74: (no net) -> GND
- J8 pad 75: (no net) -> GND
- J8 pad 76: (no net) -> GND
- J8 pad 77: (no net) -> GND
- J8 pad 78: (no net) -> GND
- J8 pad 79: (no net) -> GND
- J8 pad 8: (no net) -> GND
- J8 pad 80: (no net) -> GND
- J8 pad 81: (no net) -> GND
- J8 pad 82: (no net) -> GND
- J8 pad 83: (no net) -> GND
- J8 pad 84: (no net) -> GND
- J8 pad 85: (no net) -> GND
- J8 pad 86: (no net) -> GND
- J8 pad 87: (no net) -> GND
- J8 pad 88: (no net) -> GND
- J8 pad 89: (no net) -> GND
- J8 pad 9: (no net) -> GND
- J8 pad 90: (no net) -> GND
- J8 pad 91: (no net) -> GND
- J8 pad 92: (no net) -> GND
- J8 pad 93: (no net) -> GND
- J8 pad 94: (no net) -> GND
- J8 pad 95: (no net) -> GND
- J8 pad 96: (no net) -> GND
- J8 pad 97: (no net) -> GND
- J8 pad 98: (no net) -> GND
- J8 pad 99: (no net) -> GND
- J9 pad 1: (no net) -> GND
- J9 pad 10: (no net) -> GND
- J9 pad 100: (no net) -> GND
- J9 pad 11: (no net) -> GND
- J9 pad 12: (no net) -> GND
- J9 pad 13: (no net) -> GND
- J9 pad 14: (no net) -> GND
- J9 pad 15: (no net) -> GND
- J9 pad 16: (no net) -> GND
- J9 pad 17: (no net) -> GND
- J9 pad 18: (no net) -> GND
- J9 pad 19: (no net) -> GND
- J9 pad 2: (no net) -> GND
- J9 pad 20: (no net) -> GND
- J9 pad 21: (no net) -> GND
- J9 pad 22: (no net) -> GND
- J9 pad 23: (no net) -> GND
- J9 pad 24: (no net) -> GND
- J9 pad 25: (no net) -> GND
- J9 pad 26: (no net) -> GND
- J9 pad 27: (no net) -> GND
- J9 pad 28: (no net) -> GND
- J9 pad 29: (no net) -> GND
- J9 pad 3: (no net) -> GND
- J9 pad 30: (no net) -> GND
- J9 pad 31: (no net) -> GND
- J9 pad 32: (no net) -> GND
- J9 pad 33: (no net) -> GND
- J9 pad 34: (no net) -> GND
- J9 pad 35: (no net) -> GND
- J9 pad 36: (no net) -> GND
- J9 pad 37: (no net) -> GND
- J9 pad 38: (no net) -> GND
- J9 pad 39: (no net) -> GND
- J9 pad 4: (no net) -> GND
- J9 pad 40: (no net) -> GND
- J9 pad 41: (no net) -> GND
- J9 pad 42: (no net) -> GND
- J9 pad 43: (no net) -> GND
- J9 pad 44: (no net) -> GND
- J9 pad 45: (no net) -> GND
- J9 pad 46: (no net) -> GND
- J9 pad 47: (no net) -> GND
- J9 pad 48: (no net) -> GND
- J9 pad 49: (no net) -> GND
- J9 pad 5: (no net) -> GND
- J9 pad 50: (no net) -> GND
- J9 pad 51: (no net) -> GND
- J9 pad 52: (no net) -> GND
- J9 pad 53: (no net) -> GND
- J9 pad 54: (no net) -> GND
- J9 pad 55: (no net) -> GND
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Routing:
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- added copper zone on B.Cu, net GND
- added copper zone on F.Cu, net GND
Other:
- board size 60 x 90.8 mm -> 100 x 40.1 mm
